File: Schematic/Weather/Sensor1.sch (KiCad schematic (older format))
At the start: 6 parts, among them J11 Conn_01x04_Female, J12 Conn_01x05_Female, J13 Conn_01x04_Male, J14 Conn_01x05_Male

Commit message: more changes
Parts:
- removed J11: Conn_01x04_Female, Connector_PinHeader_2.54mm:PinHeader_1x04_P2.54mm_Vertical, symbol Connector:Conn_01x04_Female
- removed J12: Conn_01x05_Female, Connector_PinHeader_2.54mm:PinHeader_1x05_P2.54mm_Vertical, symbol Connector:Conn_01x05_Female
- removed J13: Conn_01x04_Male, Connector_PinHeader_2.54mm:PinHeader_1x04_P2.54mm_Vertical, symbol Connector:Conn_01x04_Male
- removed MOD1: HTU21, footprint:HTU21, symbol Weather-rescue:HTU21-MyComponents
- removed MOD2: BMP180, footprint:BMP180, symbol MyComponents:BMP180
- added MOD1: HTU21, footprint:HTU21, symbol MyComponents:HTU21
- renumbered J14 to J2
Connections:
- wire segments 34 -> 0
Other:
- moved on the sheet: J2
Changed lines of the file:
@@
 $Descr A4 11693 8268
 encoding utf-8
-Sheet 4 14
+Sheet 4 15
 Title ""
 Date ""
@@
 Comment4 ""
 $EndDescr
-Text HLabel 3000 2650 0    50   Input ~ 0
+Text HLabel 3050 2650 0    50   Input ~ 0
 J4_P1
-Text HLabel 3000 2800 0    50   Input ~ 0
+Text HLabel 3050 2800 0    50   Input ~ 0
 J4_P2
-Text HLabel 3000 2950 0    50   Input ~ 0
+Text HLabel 3050 2950 0    50   Input ~ 0
 J4_P3
-Text HLabel 3000 3100 0    50   Input ~ 0
+Text HLabel 3050 3100 0    50   Input ~ 0
 J4_P4
-Wire Wire Line
-	4350 2650 3000 2650
-Wire Wire Line
-	3000 3100 4050 3100
-Wire Wire Line
-	3000 2950 3350 2950
-Wire Wire Line
-	3350 2950 3350 3300
-Wire Wire Line
-	3350 3300 4900 3300
-Wire Wire Line
-	3000 2800 3650 2800
-Wire Wire Line
-	3650 2800 3650 3200
-Wire Wire Line
-	3650 3200 5000 3200
-Wire Wire Line
-	5000 3200 5000 3650
-Wire Wire Line
-	4050 4100 4050 3100
-Connection ~ 4050 3100
-Wire Wire Line
-	4900 3800 4900 3300
-Connection ~ 4900 3300
-Wire Wire Line
-	4900 3300 5150 3300
-Wire Wire Line
-	4350 3950 4350 3000
 $Comp
-L Connector:Conn_01x04_Male J13
-U 1 1 5CAF11D2
-P 6950 3000
-F 0 "J13" H 7000 3200 50  0000 C CNN
-F 1 "Conn_01x04_Male" H 7150 3350 50  0000 C CNN
-F 2 "Connector_PinHeader_2.54mm:PinHeader_1x04_P2.54mm_Vertical" H 6950 3000 50  0001 C CNN
-F 3 "~" H 6950 3000 50  0001 C CNN
-	1    6950 3000
+L Connector:Conn_01x05_Male J2
+U 1 1 5CAF34CD
+P 7000 4050
+F 0 "J2" H 7150 4400 50  0000 R CNN
+F 1 "Conn_01x05_Male" H 7650 4650 50  0000 R CNN
+F 2 "Connector_PinHeader_2.54mm:PinHeader_1x05_P2.54mm_Vertical" H 7000 4050 50  0001 C CNN
+F 3 "~" H 7000 4050 50  0001 C CNN
+	1    7000 4050
 	1    0    0    1
 $EndComp
 $Comp
-L Connector:Conn_01x05_Male J14
-U 1 1 5CAF34CD
-P 6950 4050
-F 0 "J14" H 7100 4400 50  0000 R CNN
-F 1 "Conn_01x05_Male" H 7600 4650 50  0000 R CNN
-F 2 "Connector_PinHeader_2.54mm:PinHeader_1x05_P2.54mm_Vertical" H 6950 4050 50  0001 C CNN
-F 3 "~" H 6950 4050 50  0001 C CNN
-	1    6950 4050
-	1    0    0    1
-$EndComp
-Wire Wire Line
-	5250 3950 4350 3950
-Wire Wire Line
-	5250 3800 4900 3800
-Wire Wire Line
-	5000 3650 5250 3650
-Wire Wire Line
-	5250 4100 4050 4100
-$Comp
-L Weather-rescue:HTU21-MyComponents MOD?
-U 1 1 5C959FE9
-P 7650 4050
-AR Path="/5C959FE9" Ref="MOD?"  Part="1"
-AR Path="/5C9254A0/5C959FE9" Ref="MOD1"  Part="1"
-F 0 "MOD1" H 8278 4046 50  0000 L CNN
-F 1 "HTU21" H 8278 3955 50  0000 L CNN
-F 2 "footprint:HTU21" H 7850 3750 50  0001 C CNN
-F 3 "" H 7850 3750 50  0001 C CNN
-	1    7650 4050
+L MyComponents:HTU21 MOD1
+U 1 1 5CB25268
+P 7900 4050
+F 0 "MOD1" H 8528 4046 50  0000 L CNN
+F 1 "HTU21" H 8528 3955 50  0000 L CNN
+F 2 "footprint:HTU21" H 8100 3750 50  0001 C CNN
+F 3 "" H 8100 3750 50  0001 C CNN
+	1    7900 4050
 	1    0    0    -1
 $EndComp
-$Comp
-L MyComponents:BMP180 MOD2
-U 1 1 5C958DD2
-P 7650 2850
-F 0 "MOD2" H 8278 2771 50  0000 L CNN
-F 1 "BMP180" H 8278 2680 50  0000 L CNN
-F 2 "footprint:BMP180" H 7850 2350 50  0001 C CNN
-F 3 "" H 7850 2350 50  0001 C CNN
-	1    7650 2850
-	1    0    0    -1
-$EndComp
-$Comp
-L Connector:Conn_01x04_Female J11
-U 1 1 5CAF0516
-P 6700 3000
-F 0 "J11" H 6550 2700 50  0000 L CNN
-F 1 "Conn_01x04_Female" H 5950 2600 50  0000 L CNN
-F 2 "Connector_PinHeader_2.54mm:PinHeader_1x04_P2.54mm_Vertical" H 6700 3000 50  0001 C CNN
-F 3 "~" H 6700 3000 50  0001 C CNN
-	1    6700 3000
-	1    0    0    1
-$EndComp
-Connection ~ 5000 3200
-Wire Wire Line
-	4050 3100 6500 3100
-Wire Wire Line
-	7150 3100 7350 3100
-Wire Wire Line
-	7350 3100 7350 3200
-Wire Wire Line
-	7350 3200 7550 3200
-Wire Wire Line
-	7150 3000 7450 3000
-Wire Wire Line
-	7450 3000 7450 3050
-Wire Wire Line
-	7450 3050 7550 3050
-Wire Wire Line
-	7150 2900 7550 2900
-Wire Wire Line
-	7150 2800 7450 2800
-Wire Wire Line
-	7450 2800 7450 2750
-Wire Wire Line
-	7450 2750 7550 2750
-Wire Wire Line
-	6500 3000 4350 3000
-Connection ~ 4350 3000
-Wire Wire Line
-	5000 2800 5000 3200
-Wire Wire Line
-	5150 2900 5150 3300
-Wire Wire Line
-	6500 2900 5150 2900
-Wire Wire Line
-	4350 2650 4350 3000
-Wire Wire Line
-	5000 2800 6500 2800
-$Comp
-L Connector:Conn_01x05_Female J12
-U 1 1 5CAF2250
-P 6750 4050
-F 0 "J12" H 6650 3700 50  0000 C CNN
-F 1 "Conn_01x05_Female" H 6350 3550 50  0000 C CNN
-F 2 "Connector_PinHeader_2.54mm:PinHeader_1x05_P2.54mm_Vertical" H 6750 4050 50  0001 C CNN
-F 3 "~" H 6750 4050 50  0001 C CNN
-	1    6750 4050
-	1    0    0    1
-$EndComp
 $EndSCHEMATC

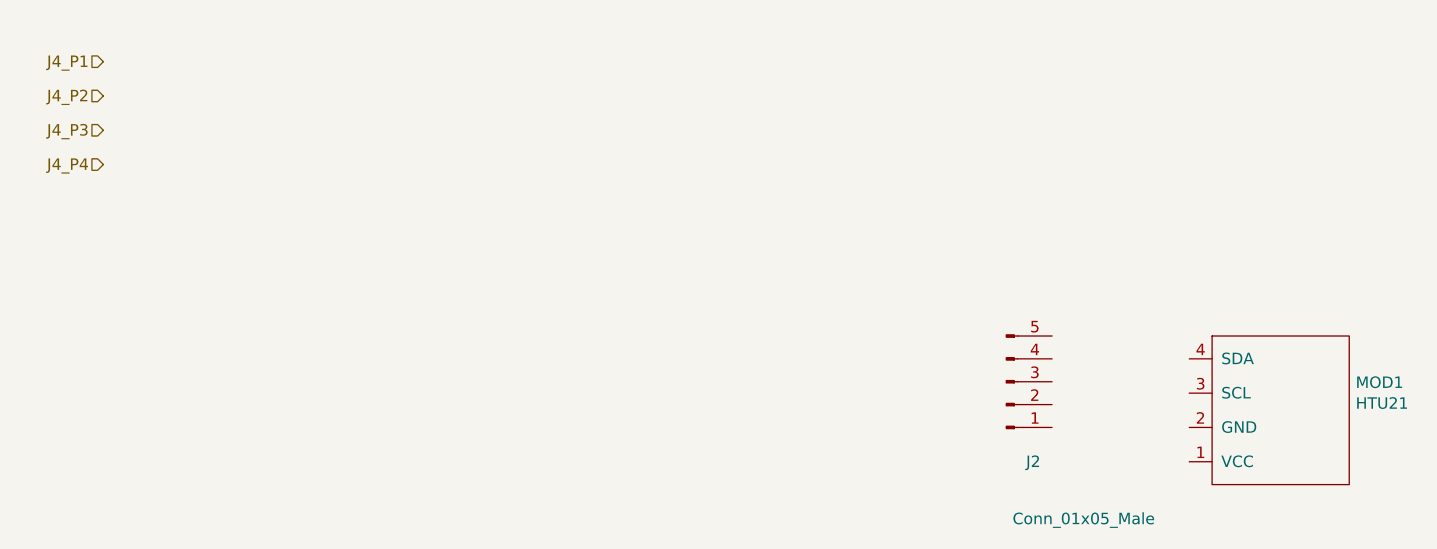
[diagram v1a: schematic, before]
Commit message: Connector relable start
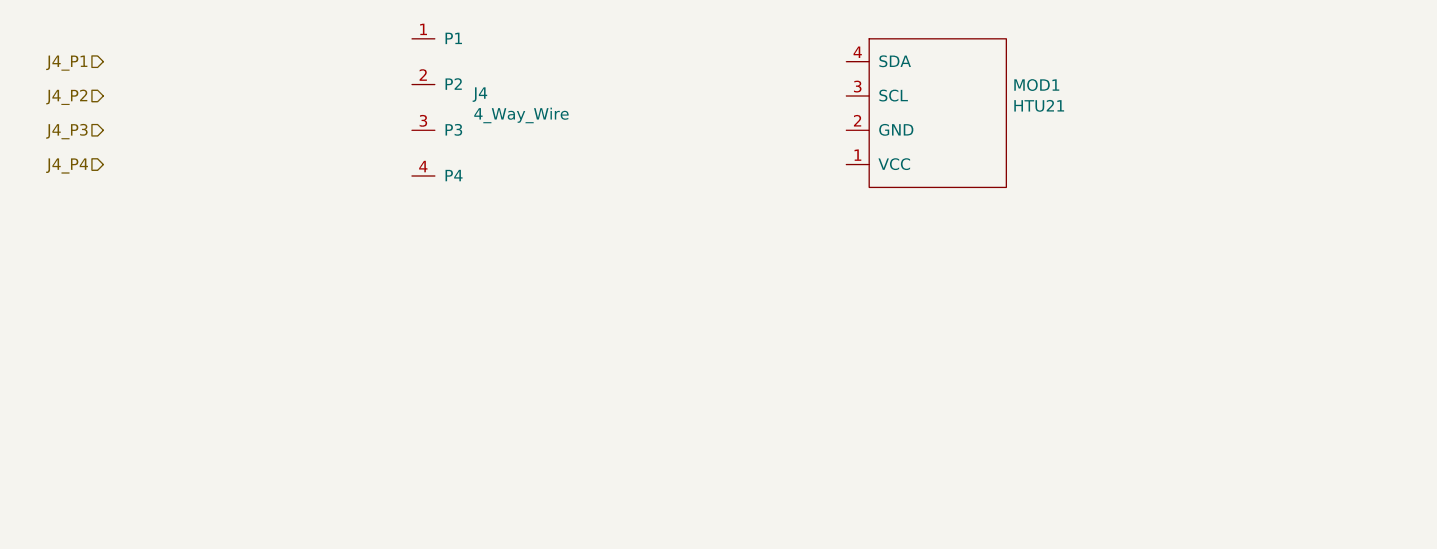
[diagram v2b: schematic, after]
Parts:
- removed J2: Conn_01x05_Male, Connector_PinHeader_2.54mm:PinHeader_1x05_P2.54mm_Vertical, symbol Connector:Conn_01x05_Male
- added J4: 4_Way_Wire, symbol MyComponents:4_Way_Wire
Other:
- moved on the sheet: MOD1
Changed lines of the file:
@@
 J4_P4
-$Comp
-L Connector:Conn_01x05_Male J2
-U 1 1 5CAF34CD
-P 7000 4050
-F 0 "J2" H 7150 4400 50  0000 R CNN
-F 1 "Conn_01x05_Male" H 7650 4650 50  0000 R CNN
-F 2 "Connector_PinHeader_2.54mm:PinHeader_1x05_P2.54mm_Vertical" H 7000 4050 50  0001 C CNN
-F 3 "~" H 7000 4050 50  0001 C CNN
-	1    7000 4050
-	1    0    0    1
-$EndComp
 $Comp
 L MyComponents:HTU21 MOD1
 U 1 1 5CB25268
-P 7900 4050
-F 0 "MOD1" H 8528 4046 50  0000 L CNN
-F 1 "HTU21" H 8528 3955 50  0000 L CNN
-F 2 "footprint:HTU21" H 8100 3750 50  0001 C CNN
-F 3 "" H 8100 3750 50  0001 C CNN
-	1    7900 4050
+P 6400 2750
+F 0 "MOD1" H 7028 2746 50  0000 L CNN
+F 1 "HTU21" H 7028 2655 50  0000 L CNN
+F 2 "footprint:HTU21" H 6600 2450 50  0001 C CNN
+F 3 "" H 6600 2450 50  0001 C CNN
+	1    6400 2750
 	1    0    0    -1
 $EndComp
+$Comp
+L MyComponents:4_Way_Wire J4
+U 1 1 5CAF466F
+P 4500 2550
+F 0 "J4" H 4669 2311 50  0000 L CNN
+F 1 "4_Way_Wire" H 4669 2220 50  0000 L CNN
+F 2 "" H 4400 2600 50  0001 C CNN
+F 3 "" H 4400 2600 50  0001 C CNN
+	1    4500 2550
+	1    0    0    -1
+$EndComp

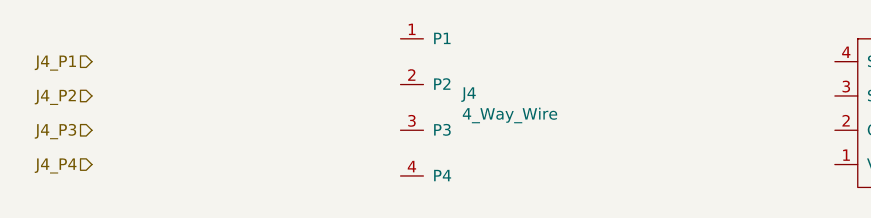
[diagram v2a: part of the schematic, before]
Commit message: Connector changes
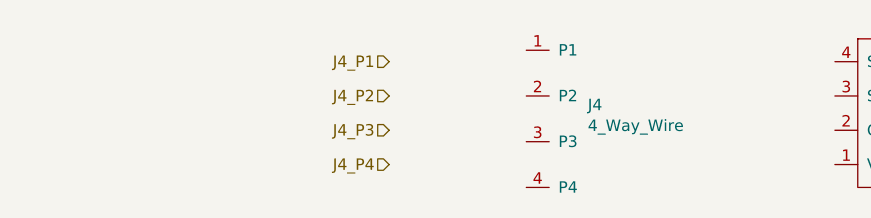
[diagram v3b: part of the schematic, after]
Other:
- moved on the sheet: J4
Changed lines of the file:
@@
 Comment4 ""
 $EndDescr
-Text HLabel 3050 2650 0    50   Input ~ 0
+Text HLabel 4350 2650 0    50   Input ~ 0
 J4_P1
-Text HLabel 3050 2800 0    50   Input ~ 0
+Text HLabel 4350 2800 0    50   Input ~ 0
 J4_P2
-Text HLabel 3050 2950 0    50   Input ~ 0
+Text HLabel 4350 2950 0    50   Input ~ 0
 J4_P3
-Text HLabel 3050 3100 0    50   Input ~ 0
+Text HLabel 4350 3100 0    50   Input ~ 0
 J4_P4
 $Comp
@@
 L MyComponents:4_Way_Wire J4
 U 1 1 5CAF466F
-P 4500 2550
-F 0 "J4" H 4669 2311 50  0000 L CNN
-F 1 "4_Way_Wire" H 4669 2220 50  0000 L CNN
-F 2 "" H 4400 2600 50  0001 C CNN
-F 3 "" H 4400 2600 50  0001 C CNN
-	1    4500 2550
+P 5050 2600
+F 0 "J4" H 5219 2361 50  0000 L CNN
+F 1 "4_Way_Wire" H 5219 2270 50  0000 L CNN
+F 2 "" H 4950 2650 50  0001 C CNN
+F 3 "" H 4950 2650 50  0001 C CNN
+	1    5050 2600
 	1    0    0    -1
 $EndComp

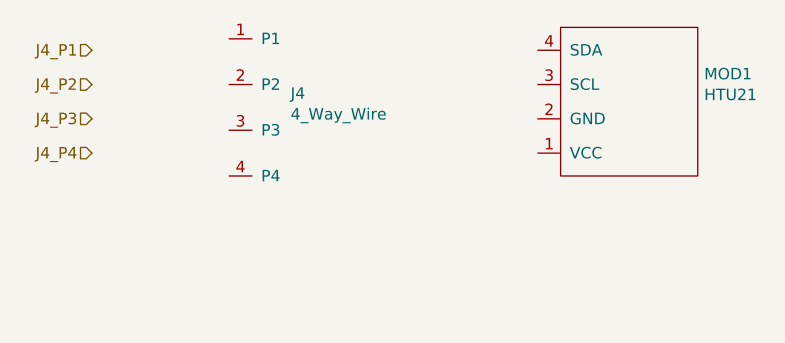
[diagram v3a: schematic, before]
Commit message: config connectors sda scl
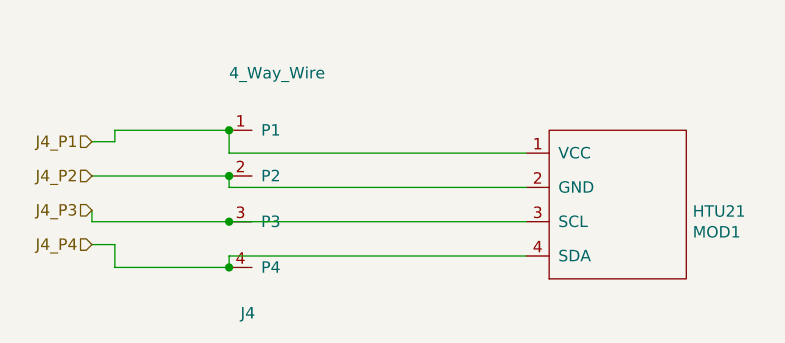
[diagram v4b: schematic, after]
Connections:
- net J4_P1: now also J4.1 (P1), MOD1.1 (VCC)
- net J4_P2: now also J4.2 (P2), MOD1.2 (GND)
- net J4_P3: now also J4.3 (P3), MOD1.3 (SCL)
- net J4_P4: now also J4.4 (P4), MOD1.4 (SDA)
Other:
- moved on the sheet: J4, MOD1
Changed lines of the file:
@@
 Comment4 ""
 $EndDescr
-Text HLabel 4350 2650 0    50   Input ~ 0
+Text HLabel 4350 3050 0    50   Input ~ 0
 J4_P1
-Text HLabel 4350 2800 0    50   Input ~ 0
+Text HLabel 4350 3200 0    50   Input ~ 0
 J4_P2
-Text HLabel 4350 2950 0    50   Input ~ 0
+Text HLabel 4350 3350 0    50   Input ~ 0
 J4_P3
-Text HLabel 4350 3100 0    50   Input ~ 0
+Text HLabel 4350 3500 0    50   Input ~ 0
 J4_P4
 $Comp
 L MyComponents:HTU21 MOD1
 U 1 1 5CB25268
-P 6400 2750
-F 0 "MOD1" H 7028 2746 50  0000 L CNN
-F 1 "HTU21" H 7028 2655 50  0000 L CNN
-F 2 "footprint:HTU21" H 6600 2450 50  0001 C CNN
-F 3 "" H 6600 2450 50  0001 C CNN
-	1    6400 2750
-	1    0    0    -1
+P 6350 3450
+F 0 "MOD1" H 6978 3446 50  0000 L CNN
+F 1 "HTU21" H 6978 3355 50  0000 L CNN
+F 2 "footprint:HTU21" H 6550 3150 50  0001 C CNN
+F 3 "" H 6550 3150 50  0001 C CNN
+	1    6350 3450
+	1    0    0    1
 $EndComp
 $Comp
 L MyComponents:4_Way_Wire J4
 U 1 1 5CAF466F
-P 5050 2600
-F 0 "J4" H 5219 2361 50  0000 L CNN
-F 1 "4_Way_Wire" H 5219 2270 50  0000 L CNN
-F 2 "" H 4950 2650 50  0001 C CNN
-F 3 "" H 4950 2650 50  0001 C CNN
-	1    5050 2600
+P 5050 3000
+F 0 "J4" H 5000 2200 50  0000 L CNN
+F 1 "4_Way_Wire" H 4950 3250 50  0000 L CNN
+F 2 "" H 4950 3050 50  0001 C CNN
+F 3 "" H 4950 3050 50  0001 C CNN
+	1    5050 3000
 	1    0    0    -1
 $EndComp
+Wire Wire Line
+	6250 3550 4950 3550
+Wire Wire Line
+	4950 3550 4950 3600
+Wire Wire Line
+	4950 3600 4450 3600
+Wire Wire Line
+	4450 3600 4450 3500
+Wire Wire Line
+	4450 3500 4350 3500
+Connection ~ 4950 3600
+Wire Wire Line
+	6250 3400 4950 3400
+Wire Wire Line
+	4950 3400 4350 3400
+Wire Wire Line
+	4350 3400 4350 3350
+Connection ~ 4950 3400
+Wire Wire Line
+	4350 3200 4950 3200
+Wire Wire Line
+	4350 3050 4450 3050
+Wire Wire Line
+	4450 3050 4450 3000
+Wire Wire Line
+	4450 3000 4950 3000
+Wire Wire Line
+	4950 3200 4950 3250
+Wire Wire Line
+	4950 3250 6250 3250
+Connection ~ 4950 3200
+Wire Wire Line
+	4950 3000 4950 3100
+Wire Wire Line
+	4950 3100 6250 3100
+Connection ~ 4950 3000
 $EndSCHEMATC

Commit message: Local webpage added
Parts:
- J4: footprint (none) -> Connector_PinSocket_2.54mm:PinSocket_1x04_P2.54mm_Vertical
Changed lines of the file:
@@
 F 0 "J4" H 5000 2200 50  0000 L CNN
 F 1 "4_Way_Wire" H 4950 3250 50  0000 L CNN
-F 2 "" H 4950 3050 50  0001 C CNN
+F 2 "Connector_PinSocket_2.54mm:PinSocket_1x04_P2.54mm_Vertical" H 4950 3050 50  0001 C CNN
 F 3 "" H 4950 3050 50  0001 C CNN
 	1    5050 3000
